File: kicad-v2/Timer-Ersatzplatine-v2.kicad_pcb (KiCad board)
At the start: 4 copper layers, 101.5 x 77.4 mm, 20 parts, among them J1 Shelly, J2 OLED SSD1306 0,91 Zoll, K1 G3VM-601AY2, SW1 Taster T1, SW2 Taster T2, SW3 Taster T3, U1 ESP32-C3 Super Mini, X1 Netz, X2 Last, X3 Snubber

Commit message: SDA geradlinig geroutet (senkrecht + eine Diagonale, wie SCL)
Der SDA-Fix-Track lief zuvor diagonal von Pad 7 quer zum OLED. Jetzt im
Hausstil: senkrecht die Pad-Spalte herunter (x=140.589) bis y=88.646,
dann eine Diagonale zu J2.4 - parallel zu SCL. DRC unveraendert sauber
(0 clearance/creepage/unrouted). Zonen neu gefuellt.

Co-Authored-By: Claude Opus 4.8 <noreply@anthropic.com>
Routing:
- net /SDA: track 32.7 -> 34.5 mm
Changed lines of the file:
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@@
 	)
 	(segment
-		(start 140.589 66.675)
-		(end 138.049 88.646)
+		(start 140.589 88.646)
+		(end 130.556 96.139)
 		(width 0.2)
 		(layer "B.Cu")
@@
 	)
 	(segment
-		(start 138.049 88.646)
-		(end 130.556 96.139)
+		(start 140.589 66.675)
+		(end 140.589 88.646)
 		(width 0.2)
 		(layer "B.Cu")

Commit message: J3-J6 + Neurouting (Nutzer) integriert; alle DRC-Fehler behoben; K1-SELV in GND-Flaeche
Nutzer (GUI): J3-J6 als OLED-Reserve-Header rechts neben J2 platziert+geroutet,
F1 gedreht/versetzt, Beschriftungen korrigiert, Platine neu geroutet.

Headless-Fixes danach:
- 4 GND-Zonen neu angelegt (waren beim GUI-Routing verloren) + gefuellt
- Short /SDA<->/+3V3: +3V3-In1-Bahn im orthogonalen Jog um U1.7 gefuehrt
- Kupfer-Rand: +5V (In2) vom Dom-Schlitz weg; PMOS-Diagonale -> orthogonaler L
- Text: 'N' (B.Silk) gespiegelt, J1-Value entspiegelt
- L_F-Zufuehrung J1.3 suedlich um K1 (45-Grad-Ast, B.Cu-Unterfuehrung unter
  /SW_SHELLY mit 2 Vias, orthogonal in K1.4) -> real >=6mm von K1.2
- GND-Flaechen-Ecke zurueck auf (185,97): K1-SELV-Seite (K1.1 Aussparung,
  K1.2 angebunden) IN der Flaeche

DRC: 0 echte Fehler (nur 4 Silk-Rand-Hinweise + 24 lib_footprint), 0 unrouted.
Doku/Projektplan/Handbuch-Renders nachgezogen, PDFs neu.

Co-Authored-By: Claude Opus 4.8 <noreply@anthropic.com>
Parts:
- added J3: OLED SSD1306 0,91 Zoll, Connector_PinHeader_2.54mm:PinHeader_1x04_P2.54mm_Vertical, F.Cu at (135.0, 88.5)
- added J4: OLED SSD1306 0,91 Zoll, Connector_PinHeader_2.54mm:PinHeader_1x04_P2.54mm_Vertical, F.Cu at (139.6, 88.5)
- added J5: OLED SSD1306 0,91 Zoll, Connector_PinHeader_2.54mm:PinHeader_1x04_P2.54mm_Vertical, F.Cu at (144.2, 88.5)
- added J6: OLED SSD1306 0,91 Zoll, Connector_PinHeader_2.54mm:PinHeader_1x04_P2.54mm_Vertical, F.Cu at (148.8, 88.5)
- J1: value Shelly -> 250-204
- moved F1 4.27 mm to (166.0, 105.5), turned to -90 degrees
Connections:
- F1 pad 1: /L_F -> /L_IN
- F1 pad 2: /L_IN -> /L_F
- K1 pad 3: /L_F -> /SW_SHELLY
- K1 pad 4: /SW_SHELLY -> /L_F
- PS1 pad 1: /N -> /L_F
- PS1 pad 2: /L_F -> /N
- RV1 pad 1: /L_F -> /N
- RV1 pad 2: /N -> /L_F
- X1 pad 1: /N -> /L_IN
- X1 pad 2: /L_IN -> /N
- X3 pad 1: /O_LAST -> /N
- X3 pad 2: /N -> /O_LAST
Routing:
- net /+3V3: track 43.8 -> 60.9 mm
- net /SCL: track 29.0 -> 45.9 mm
- net GND: track 159.8 -> 173.8 mm
- net /SDA: track 34.5 -> 48.3 mm
- net /SW_SHELLY: track 36.8 -> 26.3 mm
- net /N: track 106.4 -> 98.5 mm
- net /O_LAST: track 46.6 -> 53.0 mm
- net /L_F: track 79.3 -> 85.0 mm, vias 0 -> 2
- net /PMOS_DRV: track 27.9 -> 30.0 mm
- net /L_IN: track 17.2 -> 15.7 mm, vias 1 -> 0
- net /BTN1: track 56.0 -> 55.3 mm
- net /+5V: track 114.6 -> 114.1 mm, vias 0 -> 3
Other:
- board text added: "Feeder-Relais V2.0.1"
- board text added: "L"
- board text added: "Last"
- board text added: "N"
- board text added: "O"
- board text added: "SW"
- board text added: "Shelly 1PM mini"
- board text added: "© S.Sternitzke 08/2026"
- board text removed: "Feeder-Relais V0.1.1"
- board text removed: "© S.Sternitzke 07/2026"

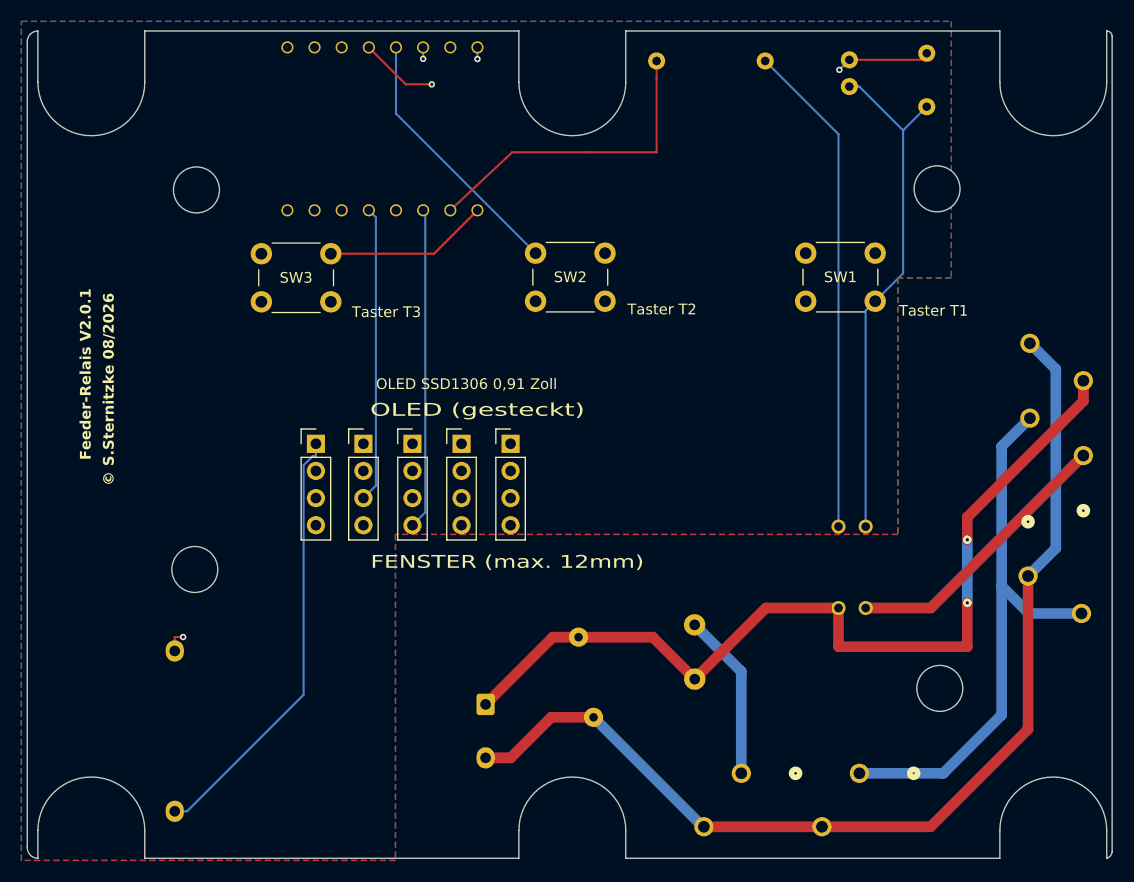
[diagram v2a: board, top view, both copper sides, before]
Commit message: Dom-Schlitze Ø10 -> Ø11 (rechte zwei asymmetrisch), Attrappe + Doku nach
- 4 Schlitze symmetrisch r5->5.5 (Waende +-0.5, Boden +0.5); linke Ecken-
  boegen an neue Waende angepasst (Schnittpunkte berechnet)
- 2 rechte Schlitze asymmetrisch: innen/Boden +0.5, Aussenwand bleibt an
  x=204.546 - zur Board-Kante (205.05) sind nur 0.5mm Material, jede
  Verbreiterung nach aussen ergaebe einen unfertigbaren Haarsteg
- +5V(In2)/PMOS(F.Cu)-Bahnen unterm oberen Mittelschlitz auf y=61.45
  (Schlitzboden jetzt 60.198)
- Kontur geschlossen (1 Outline), Mass unveraendert 101.6x77.5, DRC ohne
  echte Fehler, 0 unrouted
- box/Timer-Ersatzplatine-v2-BOARD.stl (Anprobe-Attrappe) neu exportiert,
  Handbuch-Renders + alle PDFs neu

Co-Authored-By: Claude Opus 4.8 <noreply@anthropic.com>
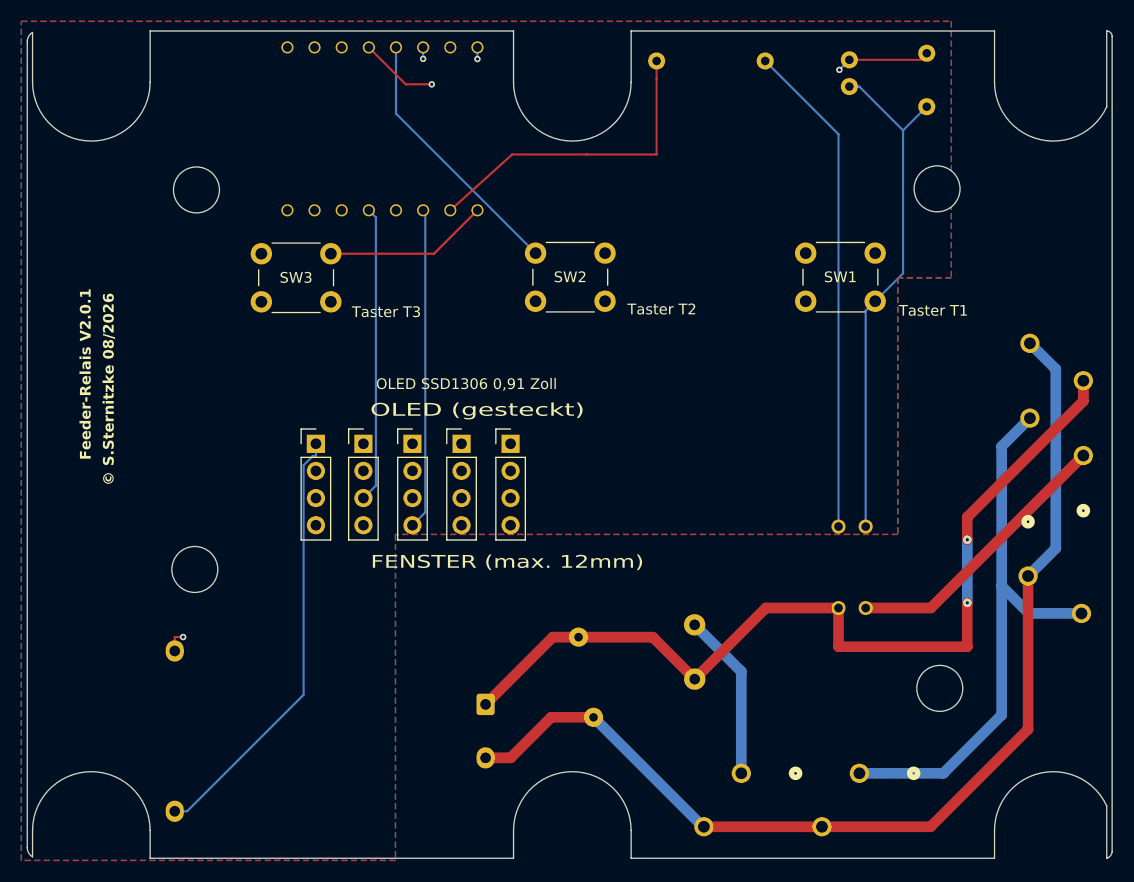
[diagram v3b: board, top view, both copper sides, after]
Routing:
- net /+5V: track 114.1 -> 114.9 mm
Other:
- outline, holes or cut-outs redrawn
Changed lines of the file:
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@@
 	(gr_arc
 		(start 103.55 50.9)
-		(mid 103.843 50.193)
-		(end 104.55 49.9)
+		(mid 103.683 50.403)
+		(end 104.046 50.036)
 		(stroke
 			(width 0.1)
@@
 	)
 	(gr_line
-		(start 104.546 49.898)
-		(end 104.546 54.698)
-		(stroke
-			(width 0.1)
-			(type solid)
-		)
-		(layer "Edge.Cuts")
-	)
-	(gr_line
-		(start 104.546 124.698)
-		(end 104.546 127.298)
+		(start 104.046 50.036)
+		(end 104.046 54.698)
+		(stroke
+			(width 0.1)
+			(type solid)
+		)
+		(layer "Edge.Cuts")
+	)
+	(gr_line
+		(start 104.046 124.698)
+		(end 104.046 127.164)
 		(stroke
 			(width 0.1)
@@
 	)
 	(gr_arc
-		(start 104.546 124.698)
-		(mid 109.546 119.698)
-		(end 114.546 124.698)
+		(start 104.046 124.698)
+		(mid 109.546 119.198)
+		(end 115.046 124.698)
 		(stroke
 			(width 0.1)
@@
 	)
 	(gr_arc
-		(start 104.55 127.3)
-		(mid 103.843 127.007)
+		(start 104.046 127.164)
+		(mid 103.682 126.797)
 		(end 103.55 126.3)
 		(stroke
@@
 	)
 	(gr_line
-		(start 114.546 49.898)
-		(end 149.546 49.898)
+		(start 115.046 49.898)
+		(end 149.046 49.898)
 		(stroke
 			(width 0.1)
@@
 	)
 	(gr_arc
-		(start 114.546 54.698)
-		(mid 109.546 59.698)
-		(end 104.546 54.698)
-		(stroke
-			(width 0.1)
-			(type solid)
-		)
-		(layer "Edge.Cuts")
-	)
-	(gr_line
-		(start 114.546 54.698)
-		(end 114.546 49.898)
-		(stroke
-			(width 0.1)
-			(type solid)
-		)
-		(layer "Edge.Cuts")
-	)
-	(gr_line
-		(start 114.546 127.298)
-		(end 114.546 124.698)
-		(stroke
-			(width 0.1)
-			(type solid)
-		)
-		(layer "Edge.Cuts")
-	)
-	(gr_line
-		(start 149.546 49.898)
-		(end 149.546 54.698)
-		(stroke
-			(width 0.1)
-			(type solid)
-		)
-		(layer "Edge.Cuts")
-	)
-	(gr_line
-		(start 149.546 124.698)
-		(end 149.546 127.298)
+		(start 115.046 54.698)
+		(mid 109.546 60.198)
+		(end 104.046 54.698)
+		(stroke
+			(width 0.1)
+			(type solid)
+		)
+		(layer "Edge.Cuts")
+	)
+	(gr_line
+		(start 115.046 54.698)
+		(end 115.046 49.898)
+		(stroke
+			(width 0.1)
+			(type solid)
+		)
+		(layer "Edge.Cuts")
+	)
+	(gr_line
+		(start 115.046 127.298)
+		(end 115.046 124.698)
+		(stroke
+			(width 0.1)
+			(type solid)
+		)
+		(layer "Edge.Cuts")
+	)
+	(gr_line
+		(start 149.046 49.898)
+		(end 149.046 54.698)
+		(stroke
+			(width 0.1)
+			(type solid)
+		)
+		(layer "Edge.Cuts")
+	)
+	(gr_line
+		(start 149.046 124.698)
+		(end 149.046 127.298)
 		(stroke
 			(width 0.1)
@@
 	)
 	(gr_arc
-		(start 149.546 124.698)
-		(mid 154.546 119.698)
-		(end 159.546 124.698)
-		(stroke
-			(width 0.1)
-			(type solid)
-		)
-		(layer "Edge.Cuts")
-	)
-	(gr_line
-		(start 149.546 127.298)
-		(end 114.546 127.298)
-		(stroke
-			(width 0.1)
-			(type solid)
-		)
-		(layer "Edge.Cuts")
-	)
-	(gr_line
-		(start 159.546 49.898)
-		(end 194.546 49.898)
+		(start 149.046 124.698)
+		(mid 154.546 119.198)
+		(end 160.046 124.698)
+		(stroke
+			(width 0.1)
+			(type solid)
+		)
+		(layer "Edge.Cuts")
+	)
+	(gr_line
+		(start 149.046 127.298)
+		(end 115.046 127.298)
+		(stroke
+			(width 0.1)
+			(type solid)
+		)
+		(layer "Edge.Cuts")
+	)
+	(gr_line
+		(start 160.046 49.898)
+		(end 194.046 49.898)
 		(stroke
 			(width 0.1)
@@
 	)
 	(gr_arc
-		(start 159.546 54.698)
-		(mid 154.546 59.698)
-		(end 149.546 54.698)
-		(stroke
-			(width 0.1)
-			(type solid)
-		)
-		(layer "Edge.Cuts")
-	)
-	(gr_line
-		(start 159.546 54.698)
-		(end 159.546 49.898)
-		(stroke
-			(width 0.1)
-			(type solid)
-		)
-		(layer "Edge.Cuts")
-	)
-	(gr_line
-		(start 159.546 127.298)
-		(end 159.546 124.698)
-		(stroke
-			(width 0.1)
-			(type solid)
-		)
-		(layer "Edge.Cuts")
-	)
-	(gr_line
-		(start 194.546 49.898)
-		(end 194.546 54.698)
-		(stroke
-			(width 0.1)
-			(type solid)
-		)
-		(layer "Edge.Cuts")
-	)
-	(gr_line
-		(start 194.546 124.698)
-		(end 194.546 127.298)
+		(start 160.046 54.698)
+		(mid 154.546 60.198)
+		(end 149.046 54.698)
+		(stroke
+			(width 0.1)
+			(type solid)
+		)
+		(layer "Edge.Cuts")
+	)
+	(gr_line
+		(start 160.046 54.698)
+		(end 160.046 49.898)
+		(stroke
+			(width 0.1)
+			(type solid)
+		)
+		(layer "Edge.Cuts")
+	)
+	(gr_line
+		(start 160.046 127.298)
+		(end 160.046 124.698)
+		(stroke
+			(width 0.1)
+			(type solid)
+		)
+		(layer "Edge.Cuts")
+	)
+	(gr_line
+		(start 194.046 49.898)
+		(end 194.046 54.698)
+		(stroke
+			(width 0.1)
+			(type solid)
+		)
+		(layer "Edge.Cuts")
+	)
+	(gr_line
+		(start 194.046 124.698)
+		(end 194.046 127.298)
 		(stroke
 			(width 0.1)
@@
 	)
 	(gr_arc
-		(start 194.546 124.698)
-		(mid 199.546 119.698)
-		(end 204.546 124.698)
-		(stroke
-			(width 0.1)
-			(type solid)
-		)
-		(layer "Edge.Cuts")
-	)
-	(gr_line
-		(start 194.546 127.298)
-		(end 159.546 127.298)
+		(start 194.046 124.698)
+		(mid 199.546 119.198)
+		(end 204.546 122.407)
+		(stroke
+			(width 0.1)
+			(type solid)
+		)
+		(layer "Edge.Cuts")
+	)
+	(gr_line
+		(start 194.046 127.298)
+		(end 160.046 127.298)
 		(stroke
 			(width 0.1)
@@
 	)
 	(gr_arc
-		(start 204.546 54.698)
-		(mid 199.546 59.698)
-		(end 194.546 54.698)
-		(stroke
-			(width 0.1)
-			(type solid)
-		)
-		(layer "Edge.Cuts")
-	)
-	(gr_line
-		(start 204.546 54.698)
+		(start 204.546 56.989)
+		(mid 199.546 60.198)
+		(end 194.046 54.698)
+		(stroke
+			(width 0.1)
+			(type solid)
+		)
+		(layer "Edge.Cuts")
+	)
+	(gr_line
+		(start 204.546 56.989)
 		(end 204.546 49.898)
 		(stroke
@@
 	(gr_line
 		(start 204.546 127.298)
-		(end 204.546 124.698)
+		(end 204.546 122.407)
 		(stroke
 			(width 0.1)
@@
 	)
 	(segment
-		(start 146.7223 60.45)
-		(end 173.0173 60.45)
+		(start 146.7223 61.45)
+		(end 173.0173 61.45)
 		(width 0.2)
 		(layer "In2.Cu")
@@
 	(segment
 		(start 146.7223 64.3428)
-		(end 146.7223 60.45)
+		(end 146.7223 61.45)
 		(width 0.2)
 		(layer "In2.Cu")
@@
 	)
 	(segment
-		(start 173.0173 60.45)
+		(start 173.0173 61.45)
 		(end 179.5295 53.5355)
 		(width 0.2)
@@
 	)
 	(segment
-		(start 146.7223 60.45)
+		(start 146.7223 61.45)
 		(end 146.7223 53.5793)
 		(width 0.2)
@@
 	)
 	(segment
-		(start 162.433 61.25)
+		(start 162.433 61.45)
 		(end 162.433 54.367)
 		(width 0.2)
@@
 	)
 	(segment
-		(start 148.9234 61.25)
-		(end 155.9195 61.25)
+		(start 148.9234 61.45)
+		(end 155.9195 61.45)
 		(width 0.2)
 		(layer "F.Cu")
@@
 	)
 	(segment
-		(start 155.919 61.25)
-		(end 162.433 61.25)
+		(start 155.919 61.45)
+		(end 162.433 61.45)
 		(width 0.2)
 		(layer "F.Cu")
@@
 	(segment
 		(start 143.129 66.675)
-		(end 148.9234 61.25)
-		(width 0.2)
-		(layer "F.Cu")
+		(end 148.9234 61.45)
+		(width 0.2)
+		(layer "F.Cu")
